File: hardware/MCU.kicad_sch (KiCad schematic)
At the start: 30 parts, among them Q1 2N2219, Q2 2N2219, SW2 GPIO_N_RST, SW3 SW_SYS-PWR, SW4 GPIO_HW_ADDR_SEL, U3 SX1509BIULTRT

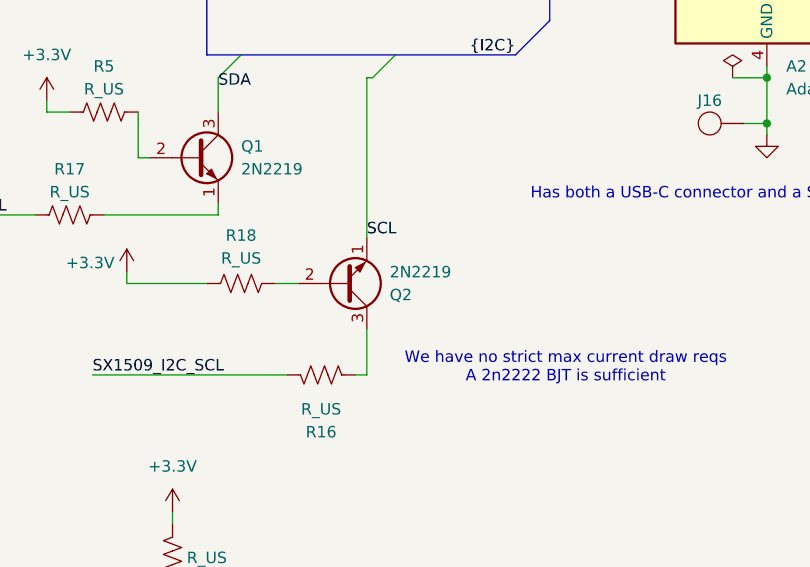
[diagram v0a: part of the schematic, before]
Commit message: fix [HWE]: Fix orientation of SX1509 SDA BJT (as Level Shifter)
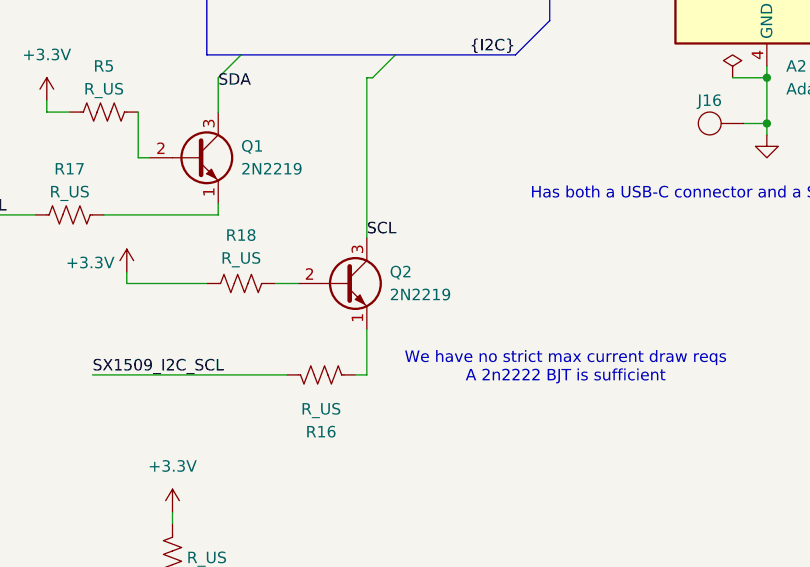
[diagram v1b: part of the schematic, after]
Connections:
- net SCL: now also Q2.3 (C); no longer Q2.1 (E)
- net at R16.2: now also Q2.1 (E); no longer Q2.3 (C)
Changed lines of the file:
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@@
 		(lib_id "Transistor_BJT:2N2219")
 		(at 158.75 130.81 0)
-		(mirror x)
 		(unit 1)
 		(exclude_from_sim no)
@@
 		(dnp no)
 		(property "Reference" "Q2"
-			(at 163.83 132.0801 0)
+			(at 163.83 129.5399 0)
 			(effects
 				(font
@@
 		)
 		(property "Value" "2N2219"
-			(at 163.83 129.5401 0)
+			(at 163.83 132.0799 0)
 			(effects
 				(font
@@
 		)
 		(property "Footprint" "Package_TO_SOT_THT:TO-39-3"
-			(at 163.83 128.905 0)
+			(at 163.83 132.715 0)
 			(effects
 				(font
